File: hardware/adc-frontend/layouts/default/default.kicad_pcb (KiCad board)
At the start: 4 copper layers, 142.2 x 111.6 mm, 135 parts

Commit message: 電源: AVDD/PLLレギュレータをRT9013-18(1.85V, SOT-23-5)へ小型化
U6を旧AZ1117H-ADJ(SOT-223, 5V直接降圧, 可変+分圧, ~0.9W)から
RT9013-18GB(固定1.85V/500mA, SOT-23-5, LCSC C59969)へ置換。
3.3Vアナログレール(p3v3_a)から供給しドロップ1.45V/損失~0.35Wに低減。
1.85VはTVP7002推奨範囲(1.8〜2.0V)内で上下マージンあり。分圧抵抗R120/R62は削除。
EN=VIN(常時ON)。EasyEDA経由でC59969を取込(parts/RICHTEK_RT9013_18GB)。
※U6はSOT-23-5へFP変更のため要再配置・再配線。

Co-Authored-By: Claude Opus 4.8 (1M context) <noreply@anthropic.com>
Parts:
- removed R12: 62Ω ±1%, FOJAN_FRC0402F62R0TS:R0402
- removed R13: 120Ω ±1%, UNI_ROYAL_0402WGF1200TCE:R0402
- U6: footprint DIODES_AZ1117H_ADJTRE1:SOT-223-3_L6.5-W3.4-P2.30-LS7.0-BR -> RICHTEK_RT9013_18GB:SOT-23-5_L3.0-W1.7-P0.95-LS2.8-BR
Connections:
- U6 pad 1: adj -> p3v3_a-hv
- U6 pad 2: p1v9_a-hv -> gnd
- U6 pad 3: power_5v-hv -> p3v3_a-hv
- U6 pad 4: p1v9_a-hv -> (no net)

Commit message: hardware: ステータス表示用 SSD1306 I2C OLEDヘッダ(J3)を追加
- HeaderOled(1x4 2.54mm, GND/VDD/SCK/SDA, 手実装DNP)を追加。
- 既存I2Cバス(TVP7002共有)+3.3V+GNDへ結線。OLED既定0x3Cで他と非衝突。
- 追加FPGA GPIO不要。表示ロジックはgateware側で別途実装予定。

Co-Authored-By: Claude Opus 4.8 (1M context) <noreply@anthropic.com>
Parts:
- added J3: , _mech:Header_1x4_P2.54mm, F.Cu at (0.00, 0.00)
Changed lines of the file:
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@@
 		)
+	)
+	(footprint "_mech:Header_1x4_P2.54mm"
+		(layer "F.Cu")
+		(at 0 0 0)
+		(descr "Generic 4x1 2.54mm pin header, hand-soldered (not JLC-assembled). Pad numbering standard; verify orientation vs EXT board before layout.")
+		(property "Reference" "J3"
+			(at -1.6 0 0)
+			(layer "F.SilkS")
+			(effects
+				(font
+					(size 1 1)
+					(thickness 0.15)
+				)
+				(justify right)
+			)
+		)
+		(property "Value" ""
+			(at 0 3 0)
+			(layer "F.Fab")
+			(effects
+				(font
+					(size 1 1)
+					(thickness 0.15)
+				)
+			)
+		)
+		(property "Datasheet" ""
+			(at 0 0 0)
+			(layer "F.Fab")
+			(hide yes)
+			(effects
+				(font
+					(size 1.27 1.27)
+					(thickness 0.15)
+				)
+			)
+		)
+		(property "Description" ""
+			(at 0 0 0)
+			(layer "F.Fab")
+			(hide yes)
+			(effects
+				(font
+					(size 1.27 1.27)
+					(thickness 0.15)
+				)
+			)
+		)
+		(property "atopile_address" "j_oled"
+			(at 0 0 0)
+			(layer "User.9")
+			(hide yes)
+		)
+		(attr through_hole exclude_from_pos_files)
+		(fp_line
+			(start -1.5 -1.5)
+			(end -1.5 1.5)
+			(stroke
+				(width 0.12)
+				(type solid)
+			)
+			(layer "F.SilkS")
+		)
+		(fp_line
+			(start -1.5 -1.5)
+			(end 9.12 -1.5)
+			(stroke
+				(width 0.12)
+				(type solid)
+			)
+			(layer "F.SilkS")
+		)
+		(fp_line
+			(start -1.5 1.5)
+			(end 9.12 1.5)
+			(stroke
+				(width 0.12)
+				(type solid)
+			)
+			(layer "F.SilkS")
+		)
+		(fp_line
+			(start 9.12 -1.5)
+			(end 9.12 1.5)
+			(stroke
+				(width 0.12)
+				(type solid)
+			)
+			(layer "F.SilkS")
+		)
+		(pad "1" thru_hole rect
+			(at 0 0 0)
+			(size 1.7 1.7)
+			(drill 1)
+			(layers "*.Cu" "*.Mask")
+			(remove_unused_layers no)
+			(net 63 "gnd")
+		)
+		(pad "2" thru_hole oval
+			(at 2.54 0 0)
+			(size 1.7 1.7)
+			(drill 1)
+			(layers "*.Cu" "*.Mask")
+			(remove_unused_layers no)
+			(net 130 "p3v3_io-hv")
+		)
+		(pad "3" thru_hole oval
+			(at 5.08 0 0)
+			(size 1.7 1.7)
+			(drill 1)
+			(layers "*.Cu" "*.Mask")
+			(remove_unused_layers no)
+			(net 24 "scl")
+		)
+		(pad "4" thru_hole oval
+			(at 7.62 0 0)
+			(size 1.7 1.7)
+			(drill 1)
+			(layers "*.Cu" "*.Mask")
+			(remove_unused_layers no)
+			(net 17 "sda")
+		)
+		(embedded_fonts no)
 	)
 	(segment

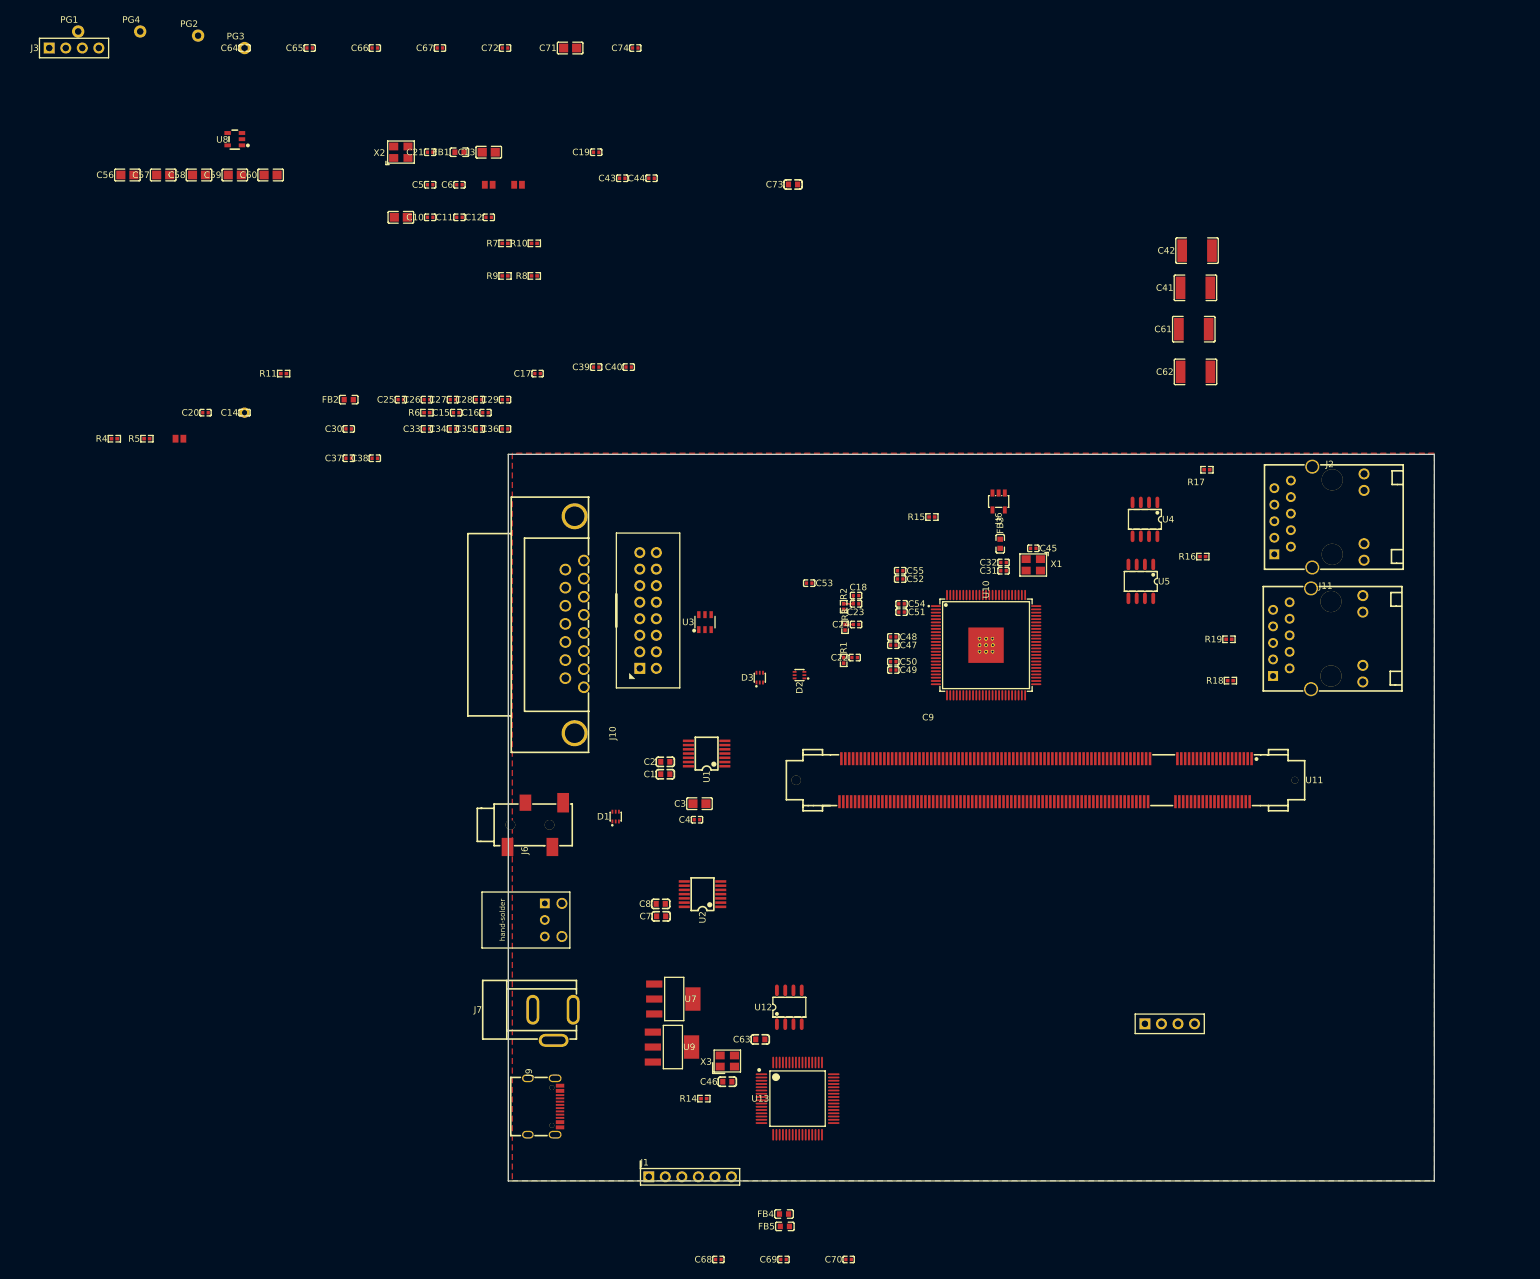
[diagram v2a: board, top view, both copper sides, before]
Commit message: hardware: RGB入力にアンチエイリアスフィルタを追加(220Ω + 33pF)
TVP7002のアナログ帯域は350〜500MHzある一方、サンプリングは8〜44MHzしかない。
ナイキストより上の雑音がそのまま折り返して絵に畳み込まれていた。TVP内蔵の帯域
制御(3Fh)は最小でも50MHz以上で、この用途には使えないため外付けが必須。

試作機に 220Ω + 15pF(実効25pF、遮断28.9MHz)を後付けして実測:
  ノイズ            40〜60%  →  3.9%
  暗部の底          9.2      →  0.01
  エッジ後のリンギング  19サンプル周期で6山  →  消滅
「暗部が暗くない」と「エッジの右に減衰しながら繰り返す像」は同一原因だった。
エッジの立ち上がりは2サンプル(58ns)で完了しており鮮鋭度の低下は見られない。

決め手はリンギングの周期がサンプルクロックを変えても「サンプル数で一定(約19)」
だったこと。アナログ共振なら時間で一定になるはずで、これで折り返しと分かった。
ケーブル長2m(往復20ns)では546nsの周期を説明できない点とも整合する。

基板の採用値は 220Ω + 33pF。TVPの入力容量10pFが並列に入るので実効43pF、遮断
16.8MHz で、最も高いモード(31kHz 768ドット)のナイキスト17.4MHzにほぼ一致する。
既存の部品(R220_0402 / C33pF_0603)で足りるので新規の型番追加は不要。

READMEに測定値と定数の選び方、ビーズを使ってはいけない理由、未使用アナログ入力の
10nF処理(未対応)を記録した。

Co-Authored-By: Claude Opus 5 (1M context) <noreply@anthropic.com>
Claude-Session: https://claude.ai/code/session_0162b9sN79AXtfsukcfLLU5Z
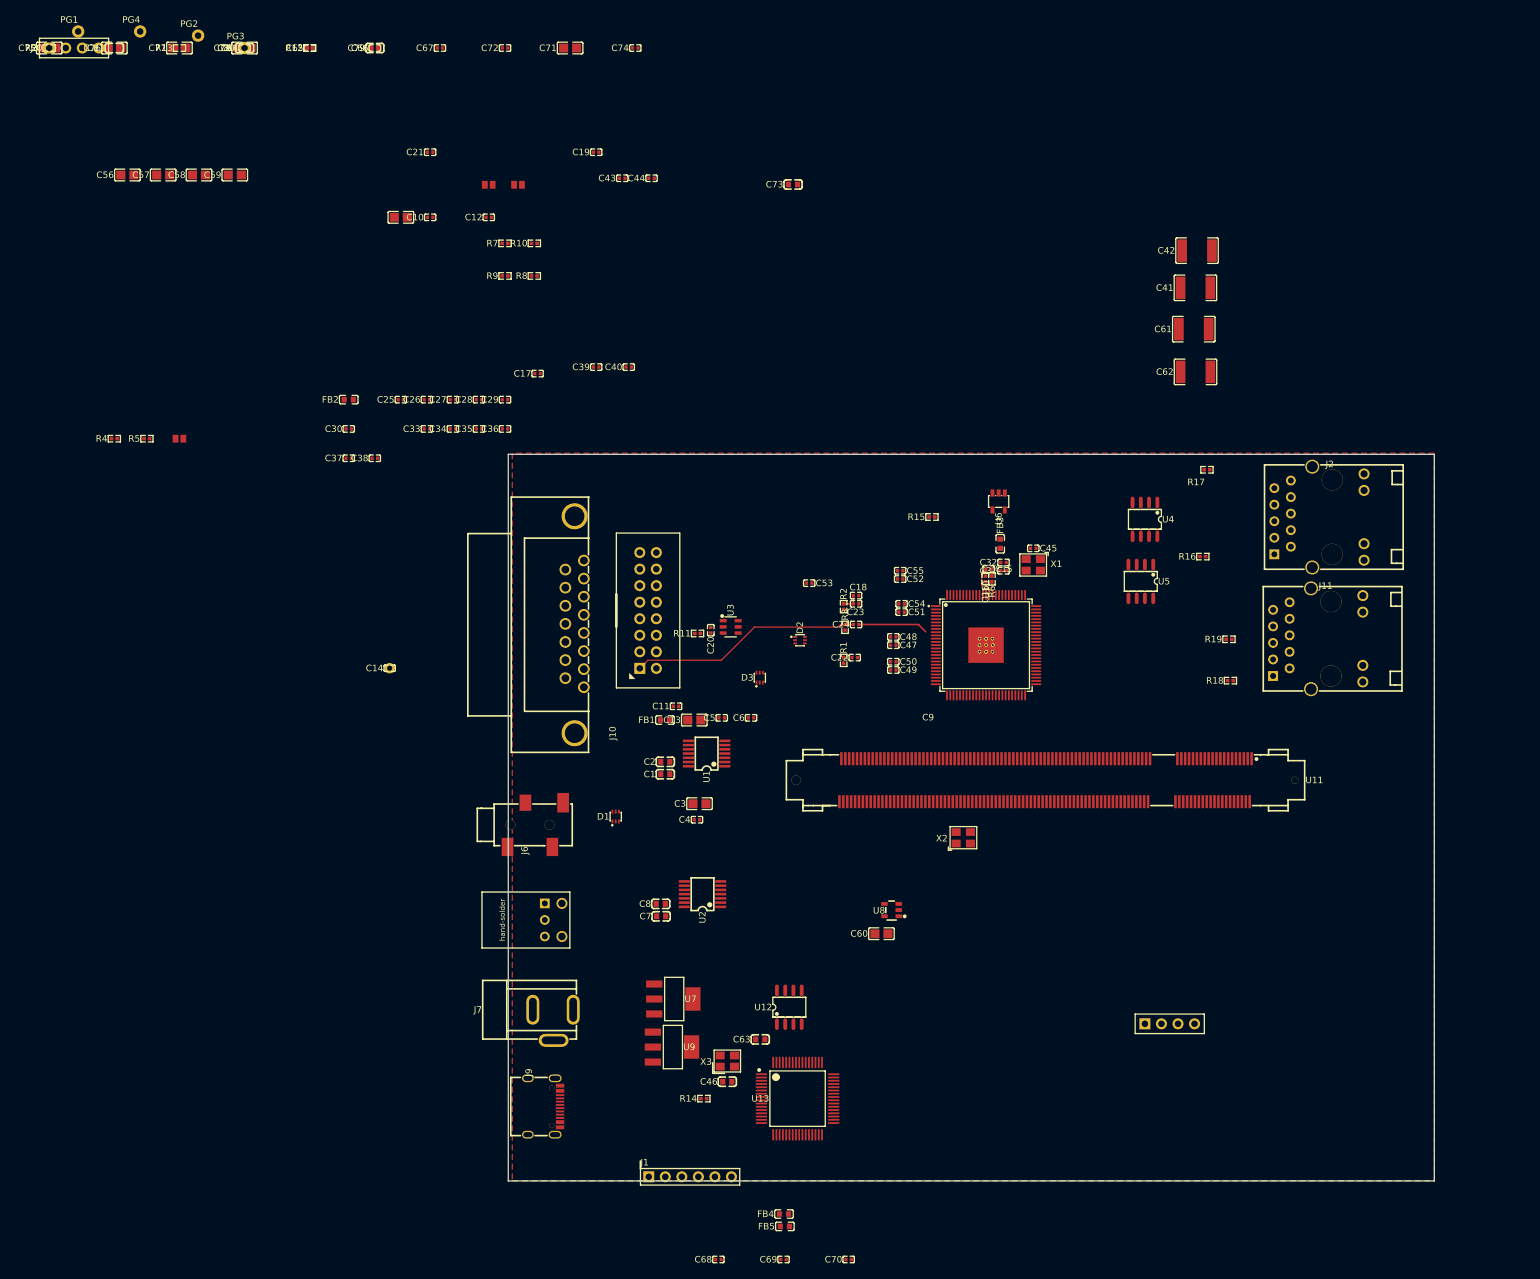
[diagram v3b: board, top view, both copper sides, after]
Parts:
- added C75: 10µF ±10%, SAMSUNG_CL21A106KAYNNNE:C0805, F.Cu at (0.00, 0.00)
- added C76: 10µF ±10%, SAMSUNG_CL21A106KAYNNNE:C0805, F.Cu at (10.0, 0.00)
- added C77: 10µF ±10%, SAMSUNG_CL21A106KAYNNNE:C0805, F.Cu at (20.0, 0.00)
- added C78: 10µF ±10%, SAMSUNG_CL21A106KAYNNNE:C0805, F.Cu at (30.0, 0.00)
- added C79: 33pF ±5%, SAMSUNG_CL10C330JB8NNNC:C0603, F.Cu at (50.0, 0.00)
- added C80: 33pF ±5%, SAMSUNG_CL10C330JB8NNNC:C0603, F.Cu at (30.0, 0.00)
- added C81: 33pF ±5%, SAMSUNG_CL10C330JB8NNNC:C0603, F.Cu at (10.0, 0.00)
- added R12: 220Ω ±1%, UNI_ROYAL_0402WGF2200TCE:R0402, F.Cu at (40.0, 0.00)
- added R13: 220Ω ±1%, UNI_ROYAL_0402WGF2200TCE:R0402, F.Cu at (20.0, 0.00)
- added R20: 220Ω ±1%, UNI_ROYAL_0402WGF2200TCE:R0402, F.Cu at (0.00, 0.00)
- moved U8 155.5 mm to (129.4, 132.4)
- moved C60 149.6 mm to (127.8, 136.0)
- moved X2 136.2 mm to (140.4, 121.3)
- moved C5 93.3 mm to (103.3, 102.9)
- moved C6 93.3 mm to (107.8, 102.9)
- moved C13 92.7 mm to (99.1, 103.2)
- moved FB1 92.7 mm to (94.6, 103.2)
- moved R6 90.5 mm to (144.8, 81.5), turned to 90 degrees
- moved C15 85.2 mm to (144.3, 80.0), turned to 180 degrees
- moved C20 84.5 mm to (101.6, 89.4), turned to 90 degrees
- moved C11 82.1 mm to (96.3, 101.1)
- moved C16 80.9 mm to (143.8, 81.5), turned to 90 degrees
- moved R11 75.1 mm to (99.6, 89.9)
- moved C14 45.1 mm to (52.3, 95.2)
- moved TP1 45.1 mm to (52.3, 95.2)
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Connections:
- net c_osci-power-hv renamed ft_osci
- net c_osco-power-hv renamed ft_osco
- net c_vregout_bulk-power-hv renamed ft_vcore_1v8
- net ct_caps[0]-power-hv renamed eth1_ct
- net ct_caps[1]-power-hv renamed eth2_ct
- net p1v9_a-hv renamed p1v9_a
- net p1v9_d-hv renamed p1v9_d
- net p3v3_a-hv renamed p3v3_a
- net power_5v-hv renamed p5v
- C11 pad 1: hv -> p5v_audio
- C12 pad 1: p3v3_io-hv -> p3v3_io
- C13 pad 1: hv -> p5v_audio
- C14 pad 1: p3v3_io-hv -> p3v3_io
- C17 pad 1: p3v3_io-hv -> p3v3_io
- C19 pad 1: p3v3_io-hv -> p3v3_io
- C21 pad 1: p3v3_io-hv -> p3v3_io
- C22 pad 2: bin3 -> lv
- C23 pad 2: gin3 -> c_ac-power-lv
- C24 pad 2: rin3 -> c_ac-power-lv-1
- C35 pad 1: p3v3_io-hv -> p3v3_io
- C36 pad 1: p3v3_io-hv -> p3v3_io
- C37 pad 1: p3v3_io-hv -> p3v3_io
- C38 pad 1: p3v3_io-hv -> p3v3_io
- C39 pad 1: p3v3_io-hv -> p3v3_io
- C40 pad 1: p3v3_io-hv -> p3v3_io
- C45 pad 1: p3v3_io-hv -> p3v3_io
- C5 pad 1: hv -> p5v_audio
- C57 pad 1: p3v3_io-hv -> p3v3_io
- C6 pad 1: p3v3_io-hv -> p3v3_io
- C64 pad 1: p3v3_io-hv -> p3v3_io
- C65 pad 1: p3v3_io-hv -> p3v3_io
- C66 pad 1: p3v3_io-hv -> p3v3_io
- C67 pad 1: p3v3_io-hv -> p3v3_io
- C69 pad 1: c_vphy-power-hv -> hv
- C71 pad 1: p3v3_io-hv -> p3v3_io
- C72 pad 1: p3v3_io-hv -> p3v3_io
- FB1 pad 2: hv -> p5v_audio
- FB4 pad 2: c_vphy-power-hv -> hv
- J1 pad 6: p3v3_io-hv -> p3v3_io
- J3 pad 2: p3v3_io-hv -> p3v3_io
- J5 pad 1: p3v3_io-hv -> p3v3_io
- J8 pad 3: p3v3_io-hv -> p3v3_io
- R10 pad 2: p3v3_io-hv -> p3v3_io
- R15 pad 2: p3v3_io-hv -> p3v3_io
- R9 pad 2: p3v3_io-hv -> p3v3_io
- U1 pad 1: audio_mclk -> aud_vref_dsub
- U1 pad 10: hv -> gnd
- U1 pad 12: aud_vref_dsub -> gnd
- U1 pad 13: aud_dsub_r_ac -> aud_dsub_l_ac
- U1 pad 14: aud_dsub_l_ac -> aud_dsub_r_ac
- U1 pad 2: audio_bck -> gnd
- U1 pad 3: audio_lrck -> p5v_audio
- U1 pad 4: gnd -> p3v3_io
- U1 pad 5: p3v3_io-hv -> gnd
- U1 pad 6: i2s_dout_dsub -> audio_mclk
- U1 pad 7: gnd -> audio_lrck
- U1 pad 8: gnd -> audio_bck
- U1 pad 9: gnd -> i2s_dout_dsub
- U10 pad 26: p3v3_io-hv -> p3v3_io
- U10 pad 41: p3v3_io-hv -> p3v3_io
- U10 pad 53: p3v3_io-hv -> p3v3_io
- U10 pad 66: p3v3_io-hv -> p3v3_io
- U11 pad 130: audio_mclk -> audio_mclk_in
- U11 pad 132: audio_bck -> 132
- U11 pad 134: audio_lrck -> 134
- U11 pad 136: i2s_dout_dsub -> 136
- U11 pad 138: i2s_dout_line -> 138
- U11 pad 139: (no net) -> i2s_dout_line
- U11 pad 141: (no net) -> i2s_dout_dsub
- U11 pad 143: (no net) -> audio_bck
- U11 pad 145: (no net) -> audio_lrck
- U11 pad 147: (no net) -> audio_mclk
- U12 pad 8: p3v3_io-hv -> p3v3_io
- U13 pad 20: p3v3_io-hv -> p3v3_io
- U13 pad 31: p3v3_io-hv -> p3v3_io
- U13 pad 4: c_vphy-power-hv -> hv
- U13 pad 42: p3v3_io-hv -> p3v3_io
- U13 pad 50: p3v3_io-hv -> p3v3_io
- U13 pad 56: p3v3_io-hv -> p3v3_io
- U2 pad 1: audio_mclk -> aud_vref_line
- U2 pad 10: hv -> gnd
- U2 pad 12: aud_vref_line -> gnd
- U2 pad 13: aud_line_r_ac -> aud_line_l_ac
- U2 pad 14: aud_line_l_ac -> aud_line_r_ac
- U2 pad 2: audio_bck -> gnd
- U2 pad 3: audio_lrck -> p5v_audio
- U2 pad 4: gnd -> p3v3_io
- U2 pad 5: p3v3_io-hv -> gnd
- U2 pad 6: i2s_dout_line -> audio_mclk
- U2 pad 7: gnd -> audio_lrck
- U2 pad 8: gnd -> audio_bck
- U2 pad 9: gnd -> i2s_dout_line
- U3 pad 5: p3v3_io-hv -> p3v3_io
- U4 pad 8: p3v3_io-hv -> p3v3_io
- U5 pad 1: p3v3_io-hv -> p3v3_io
- U5 pad 8: p3v3_io-hv -> p3v3_io
- U8 pad 1: p3v3_io-hv -> p3v3_io
- U8 pad 3: p3v3_io-hv -> p3v3_io
- U9 pad 2: p3v3_io-hv -> p3v3_io
- U9 pad 4: p3v3_io-hv -> p3v3_io
- X1 pad 1: p3v3_io-hv -> p3v3_io
- X1 pad 4: p3v3_io-hv -> p3v3_io
- X2 pad 1: p3v3_io-hv -> p3v3_io
- X2 pad 3: audio_mclk -> audio_mclk_in
- X2 pad 4: p3v3_io-hv -> p3v3_io
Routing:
- net vin_r: track 1.27 -> 35.6 mm
- net 8: track 0.00 -> 10.8 mm
- net pll_f: track 0.00 -> 5.49 mm
- net pll_filt1: track 0.00 -> 2.21 mm
- net pll_filt2: track 0.00 -> 2.18 mm
- net pll_filt_mid: track 0.00 -> 1.13 mm

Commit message: hs_offset を撤去: ラインの頭から取り込み、非黒範囲だけを絶対位置で送る
pll_divide はドットクロックの再生、つまり「1ドットをどの時点でA/D変換するか」を
決めるためのもので、絵がどこに描かれるかとは無関係でなければならない。合っていれば
ドットが綺麗に出る、ずれていれば滲む、それだけの差になるべきである。ところが
pll_divide を動かすと絵が横に跳んでいた。

原因は hs_offset がサンプル単位だったこと。サンプル k の水平位置は
(hs_offset + k)/htotal で htotal = pll_divide、k も pll_divide に比例するので式
としては時間ベースだが、hs_offset を固定したままだと取り込み開始「時刻」が変わる。

そこで hs_offset を設定項目から外した:
- キャプチャ幅を 2048 にしてラインを丸ごと保持する(15kHz 1216 / 24kHz 1408 /
  31kHz 1104 の htotal がすべて入る)。hs_offset の既定は 0
- ライン毎に「黒でない範囲」を記録し、その範囲だけを送る。ライン全体を送ると帯域が
  1.4倍になって入らない。位置は offset_px で伝える。offset_px はライン内の絶対位置
  にしたので、受信側は hs_offset を知らなくても正しい場所へ置ける
- 全黒のラインも「空の範囲」として送る。行を落とすと受信側が「黒い行」と「届かなかった
  行」を区別できず前フレームの内容が残る(インターレースのSIMがこれを捕まえた)

実機で確認: pll_divide を動かしても絵が横に動かない。lost 0、26fps/308Mbps。
バッファが 2048x1862 になりテクスチャ転送は4MB→14.5MBに増えたが欠落は出ていない。

## 行位置を半ライン単位のスロットにした

インターレースの原理は「第2フィールドのVSYNCが半ラインずれて来るので、そのライン
が第1フィールドのラインの物理的に間へ落ちる」ことである。位置を半ライン単位で
決めれば織り込みは設定無しで成立するはずなので、row_eff = fe*2 + 位相 とした。
プログレッシブでは位相が一定なのでスロットは1つ飛びに並び、空くスロットは受信側が
「次のラインまでの間隔」ぶん太らせて埋める(ビームには太さがあるので物理的にも
正しい)。埋めるのは隙間がちょうど1スロットで両隣が埋まっている場合だけにして、
送信ドロップ(不規則で幅もまちまち)と区別する。

**ただしインターレースは未完成。** 24kHz 1024x848 では il=なし にすると同じ絵が
上下に2つ出る(1VSYNC周期に2フィールド分の内容が入っている)。TVPのVSOUTは931
ラインに1パルスしか出さず、VSYNCの水平位相(vs_x)は300回読んで14に完全固定で、
同期制御レジスタ(0x0E)を256通り振っても位相は現れなかった。一方オシロで生信号を
見るとVSYNCトリガごとにHSYNCが半ラインずれる。つまり生信号にはVSYNCが2本あり、
TVPが半ライン位相を潰している。

そこで生のHSYNC/VSYNCをFPGAへ直接入れる配線を基板に追加した(hardware側)。既存の
SN74LVC2G17 の出力から分岐するだけなので新規部品は不要で、P3端子の
  pin155 (F2, クロック対応) = 生HSYNC
  pin153 (E1)               = 生VSYNC(RC遅延後)
へ引いた。これを読む実装は次の作業。それまでは il の手動設定が必要。

## タイミング

範囲計算(span_lo/span_hi/nx_off等)を組合せで書くとFIFO先頭から加算・比較・muxを
経てFSMのレジスタ入力まで伸び、sysが 48.1 → 42.4MHz へ落ちて要求45MHzを割った。
レジスタに落として回復(seed13: dataclk 100.3 / eth_rx 131.9 / sys 50.9 MHz)。
BRAMは 12/56 → 20/56 (35%)。

シードは dataclk を重視して選んだ。pll_divide 上限2304 × 31.5kHz = 72.6MHz まで
上がるので、制約75MHzに対して seed2 の 80MHz では余裕が8%しかない。

Co-Authored-By: Claude Opus 5 (1M context) <noreply@anthropic.com>
Claude-Session: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
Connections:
- U11 pad 153: 153 -> vsync_a
- U11 pad 155: 155 -> hsync_a
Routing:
- net 8: track 10.8 -> 0.00 mm
- net 129: track 0.00 -> 10.8 mm
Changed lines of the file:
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@@
 		)
 	)
-	(net 1 "vsync_a")
-	(net 2 "hsync_a")
 	(net 3 "pll_filt_mid")
 	(net 4 "pll_f")
@@
 	(net 68 "148")
 	(net 69 "154")
-	(net 70 "155")
 	(net 71 "eth2_1_N")
 	(net 72 "p5v_ext")
@@
 	(net 135 "38")
 	(net 136 "95")
-	(net 137 "153")
 	(net 138 "140")
 	(net 139 "eth-led_g_a")
@@
 	(net 168 "vd_g9")
 	(net 169 "vd_b2")
-	(net 170 "129")
 	(net 171 "vd_b9")
 	(net 172 "vd_b8")
@@
 	(net 181 "aud_dsub_r_ac")
 	(net 183 "134")
-	(net 184 "132")
 	(net 185 "aud_dsub_l_ac")
 	(net 186 "aud_line_r_ac")
@@
 	(net 201 "bin3")
 	(net 202 "rin3")
+	(net 7 "132")
+	(net 8 "129")
+	(net 1 "vsync_a")
+	(net 2 "hsync_a")
 	(footprint "UNKNOWN_TYPE_C_31_M_12:USB-C_SMD-TYPE-C-31-M-12_1"
 		(layer "F.Cu")
@@
 			(size 2 0.4)
 			(layers "F.Cu" "F.Paste" "F.Mask")
-			(net 170 "129")
+			(net 8 "129")
 		)
 		(pad "130" smd rect
@@
 			(size 2 0.4)
 			(layers "F.Cu" "F.Paste" "F.Mask")
-			(net 184 "132")
+			(net 7 "132")
 		)
 		(pad "133" smd rect
@@
 			(size 2 0.4)
 			(layers "F.Cu" "F.Paste" "F.Mask")
-			(net 137 "153")
+			(net 1 "vsync_a")
 		)
 		(pad "154" smd rect
@@
 			(size 2 0.4)
 			(layers "F.Cu" "F.Paste" "F.Mask")
-			(net 70 "155")
+			(net 2 "hsync_a")
 		)
 		(pad "156" smd rect
